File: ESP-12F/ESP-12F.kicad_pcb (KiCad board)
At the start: 2 copper layers, 30.5 x 25.4 mm, 13 parts, among them J1 Conn_01x08, J2 Conn_01x08, J3 Conn_01x06

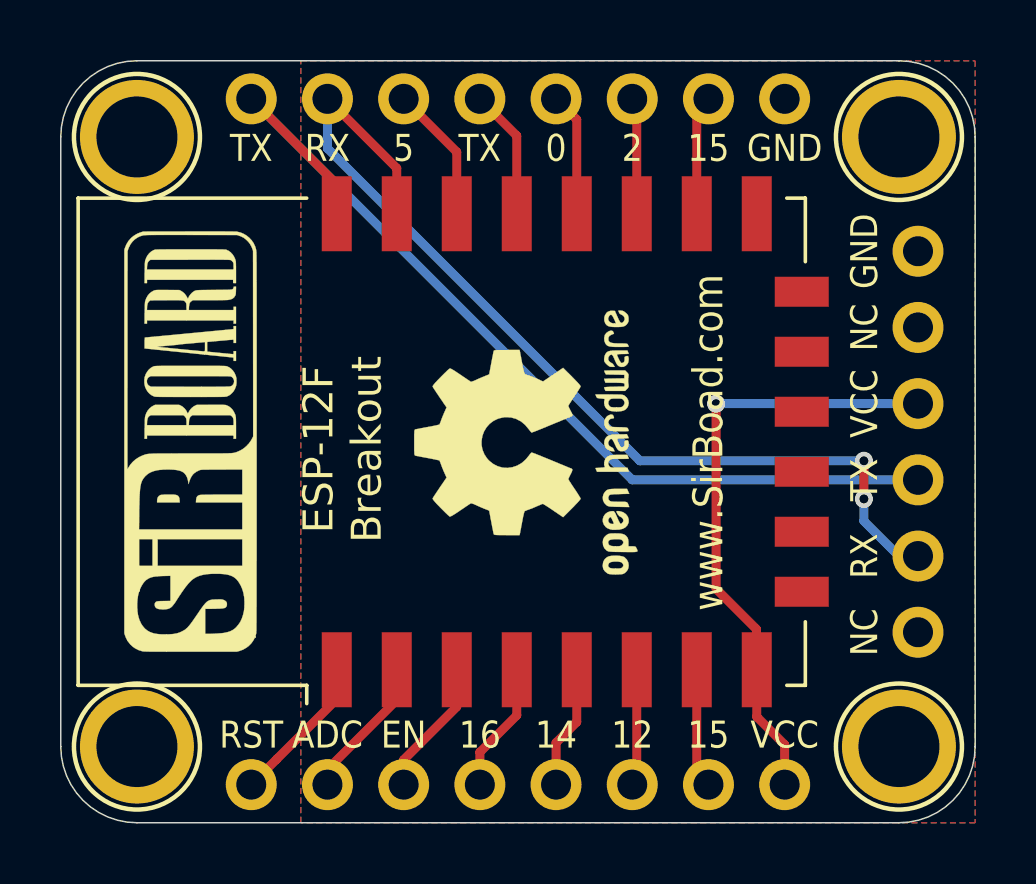
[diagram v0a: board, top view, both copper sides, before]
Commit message: ESP-12F Update
Module moved higher to allow antenna to be placed off the board.
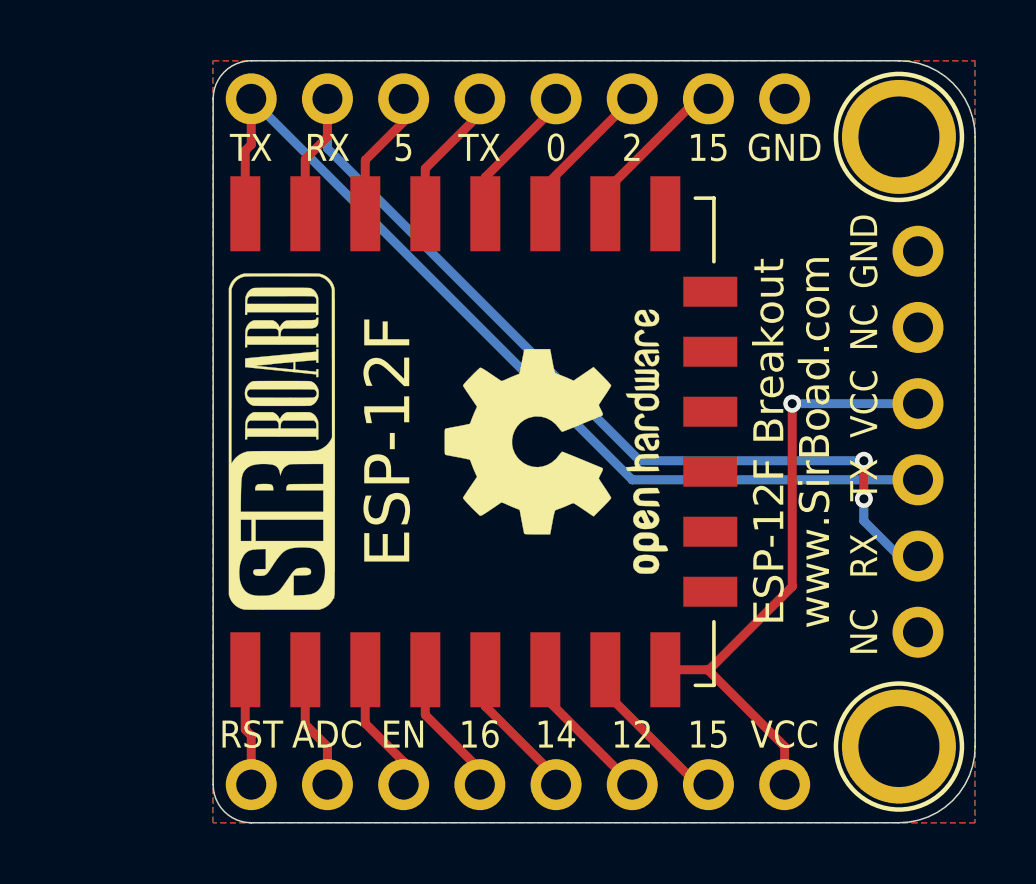
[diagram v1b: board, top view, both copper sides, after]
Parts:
- removed H1, H3: MountingHole, SirBoardLibrary:MountingHole_M2.5_SirBoard
- removed the REF** at (68.3, 38.2)
- G***: footprint logo:SirBoard140x44 -> logo:SirBoard112x35
- moved G*** 4.83 mm to (56.5, 38.2)
- moved G*** 4.70 mm to (63.6, 38.2)
- moved ESP-12F 3.05 mm to (56.0, 38.2)
- moved G*** 3.05 mm to (53.7, 38.2)
- moved REF** 1.02 mm to (62.8, 38.2)
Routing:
- net GPIO13: track 3.99 -> 5.46 mm
- net GPIO15: track 3.99 -> 5.46 mm
- net GPIO2: track 3.89 -> 5.03 mm
- net GPIO12: track 3.89 -> 5.03 mm
- net RST: track 5.01 -> 3.91 mm
- net TXD: track 32.5 -> 31.4 mm
- net GPIO0: track 4.12 -> 4.81 mm
- net GPIO14: track 4.12 -> 4.81 mm
- net ADC: track 4.79 -> 4.14 mm
- net RX: track 33.0 -> 32.3 mm
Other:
- board size 30.5 x 25.4 mm -> 25.4 x 25.4 mm
